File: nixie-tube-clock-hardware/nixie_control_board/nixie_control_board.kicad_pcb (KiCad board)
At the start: 2 copper layers, 72 x 97 mm, 66 parts, among them J1 Conn_01x07, J2 Conn_01x02_Female, P1 CONN_01X02, P2 CONN_01X02, P3 AMS1117, P5 ., Q1 IRF644, Q2 Q_PNP_BEC, SW1 SW_PUSH_SMALL, SW2 SW_PUSH_SMALL, SW3 SW_PUSH_SMALL, SW4 SW_DIP_x01, U1 DS3231, U2 AT24C02, U3 MAX1771, U4 Buzzer, U5 DHT11, U6 Logo, U7 SSD1306-OLED, U8 MP2307

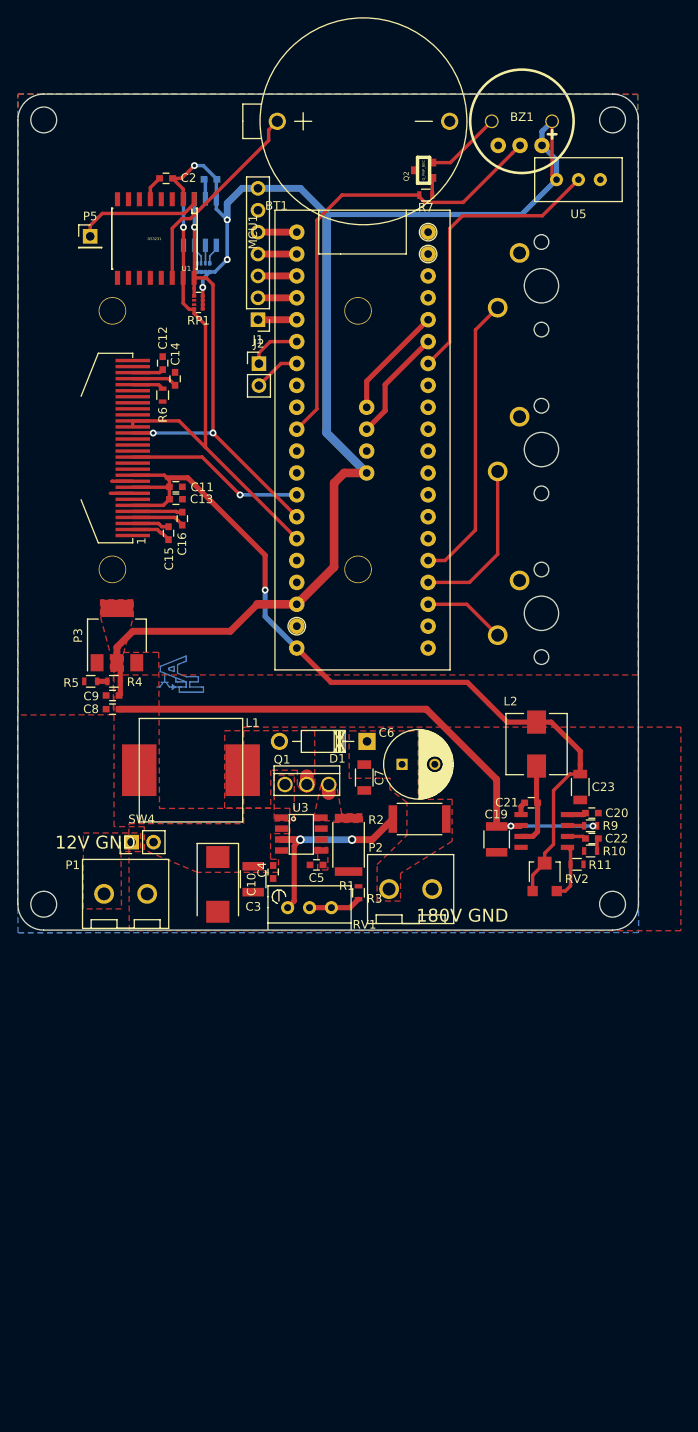
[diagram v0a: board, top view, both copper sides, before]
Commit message: Control board updated to encorporate 5v step down and 3.3v reg
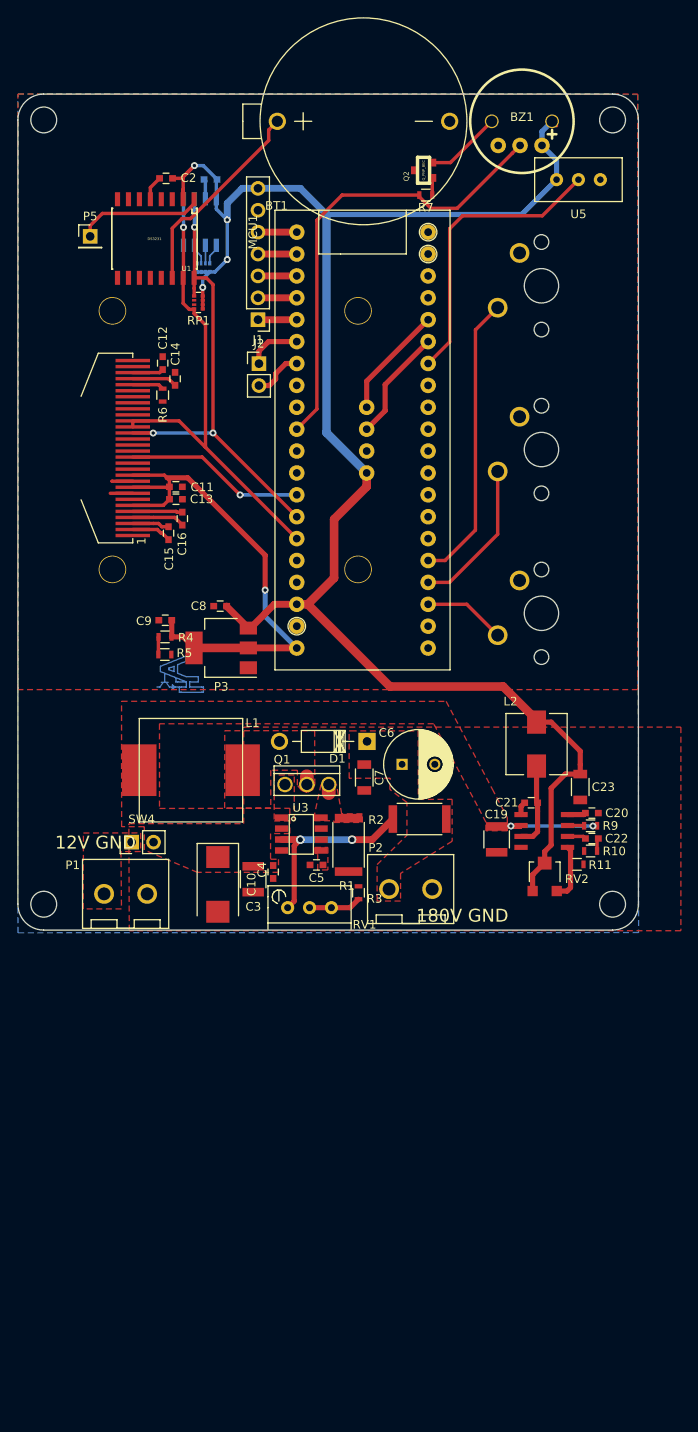
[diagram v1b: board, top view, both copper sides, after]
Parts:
- moved C8 17.3 mm to (136.5, 109.4)
- moved P3 12.2 mm to (136.6, 114.3), turned to 180 degrees
- moved C9 10.7 mm to (130.1, 111.0)
- moved R5 9.15 mm to (130.1, 115.0), turned to 0 degrees
- moved R4 7.87 mm to (130.1, 113.0)
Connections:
- C23 pad 2: +3V3 -> +5V
- C8 pad 1: +12V -> +5V
- C9 pad 1: +5V -> +3V3
- L2 pad 2: +3V3 -> +5V
- P3 pad 2: +5V -> +3V3
- P3 pad 3: +12V -> +5V
- P3 pad 4: (no net) -> +3V3
- R4 pad 1: +5V -> +3V3
- RV2 pad 1: +3V3 -> +5V
- RV2 pad 2: +3V3 -> +5V
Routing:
- net +12V: track 65.7 -> 13.0 mm
- net +3V3: track 100.0 -> 59.9 mm
- net +5V: track 171.9 -> 205.0 mm
- net BUTTON_2: track 19.0 -> 17.7 mm
- net Net-(R4-Pad2): track 1.18 -> 2.06 mm
- net BUZZER: track 53.2 -> 53.8 mm
- removed copper zone on F.Cu, net +5V

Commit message: Control board updated to be skinnier and ditch decondary through hole connections
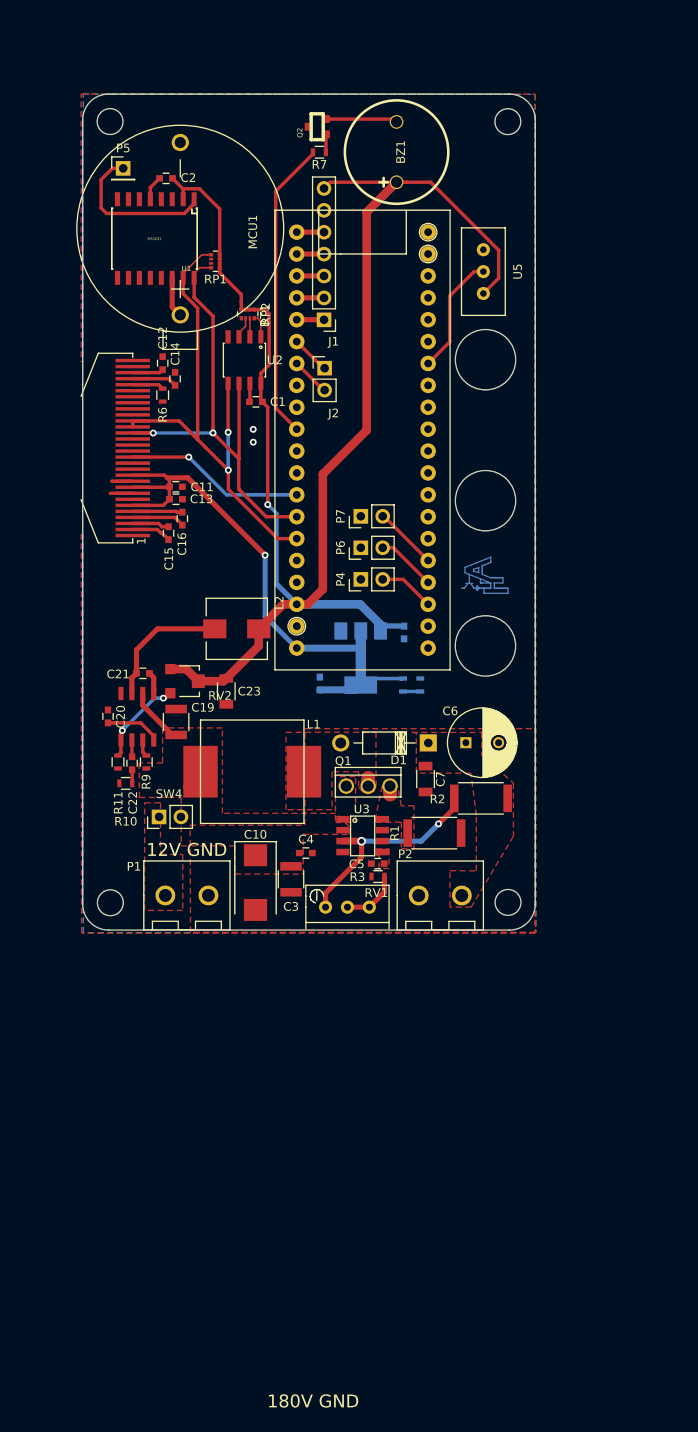
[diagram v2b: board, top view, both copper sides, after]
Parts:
- removed LCD1: 1.3_inch_LCD, keyboard:1.3_inch_LCD
- removed the REF** at (116.0, 53.0)
- removed the REF** at (116.0, 144.0)
- removed the REF** at (182.0, 144.0)
- removed SW1, SW2, SW3: SW_PUSH_SMALL, keyboard:CHERRY_PCB_100H
- removed U4: Buzzer, keyboard:Buzzer_shield
- added P4: CONN_01X02, Connector_PinHeader_2.54mm:PinHeader_1x02_P2.54mm_Vertical, F.Cu at (152.8, 106.3)
- added P6: CONN_01X02, Connector_PinHeader_2.54mm:PinHeader_1x02_P2.54mm_Vertical, F.Cu at (152.8, 102.6)
- added P7: CONN_01X02, Connector_PinHeader_2.54mm:PinHeader_1x02_P2.54mm_Vertical, F.Cu at (152.8, 99.0)
- added REF**: MountingHole_3mm, Mounting_Holes:MountingHole_3mm, F.Cu at (167.3, 97.2)
- added REF**: MountingHole_3mm, Mounting_Holes:MountingHole_3mm, F.Cu at (167.3, 80.8)
- added REF**: MountingHole_3mm, Mounting_Holes:MountingHole_3mm, F.Cu at (169.9, 143.8)
- added REF**: MountingHole_3mm, Mounting_Holes:MountingHole_3mm, F.Cu at (123.7, 143.8)
- added REF**: MountingHole_3mm, Mounting_Holes:MountingHole_3mm, F.Cu at (123.7, 53.2)
- added REF**: MountingHole_3mm, Mounting_Holes:MountingHole_3mm, F.Cu at (167.2, 114.0)
- C1, RP2, U2: moved to F.Cu
- C8, C9, P3, R4, R5: moved to B.Cu
- moved C20 57.2 mm to (123.5, 122.2), turned to 270 degrees
- moved R11 54.6 mm to (124.6, 127.5), turned to 90 degrees
- moved R10 54.5 mm to (125.5, 130.0)
- moved C22 54.1 mm to (126.2, 127.6), turned to 90 degrees
- moved R9 52.1 mm to (127.9, 127.5), turned to 270 degrees
- moved U8 49.0 mm to (126.9, 122.2), turned to 180 degrees
- moved RV2 47.6 mm to (132.3, 118.1), turned to 270 degrees
- moved C21 47.5 mm to (127.5, 117.2), turned to 0 degrees
- moved C23 42.5 mm to (137.2, 119.3)
- moved C19 39.6 mm to (131.4, 122.9), turned to 90 degrees
- moved L2 37.3 mm to (138.4, 112.0), turned to 0 degrees
- moved U6 37.2 mm to (168.9, 106.9)
- moved R5 29.9 mm to (159.7, 118.6), turned to 90 degrees
- moved R4 28.2 mm to (157.7, 118.6), turned to 270 degrees
- moved C1 26.3 mm to (140.6, 85.7)
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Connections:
- P2 pad 1: Net-(C6-Pad1) -> GND
- P2 pad 2: GND -> Net-(C6-Pad1)
- RP1 pad 5: SCL -> SDA
- RP1 pad 8: SDA -> SCL
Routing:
- net BUTTON_3: track 33.8 -> 7.39 mm
- net +5V: track 205.0 -> 178.7 mm, vias 4 -> 1
- net DHT: track 34.0 -> 13.9 mm
- net Net-(BT1-Pad1): track 23.8 -> 4.68 mm
- net BUZZER: track 53.8 -> 34.9 mm
- net SDA2: track 13.1 -> 0.00 mm
- net SCL2: track 13.1 -> 0.00 mm
- net BUTTON_2: track 17.7 -> 6.94 mm
- net +3V3: track 59.9 -> 68.8 mm
- net Net-(C21-Pad1): track 9.81 -> 15.4 mm
- net SDA: track 55.6 -> 60.9 mm, vias 1 -> 2
- net Net-(C20-Pad2): track 2.15 -> 6.40 mm
- net Net-(R11-Pad2): track 6.58 -> 10.5 mm, vias 0 -> 2
- net Net-(P5-Pad1): track 14.9 -> 18.4 mm
- net Net-(R2-Pad2): track 22.4 -> 25.0 mm
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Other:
- board size 72 x 97 mm -> 52.5 x 97 mm

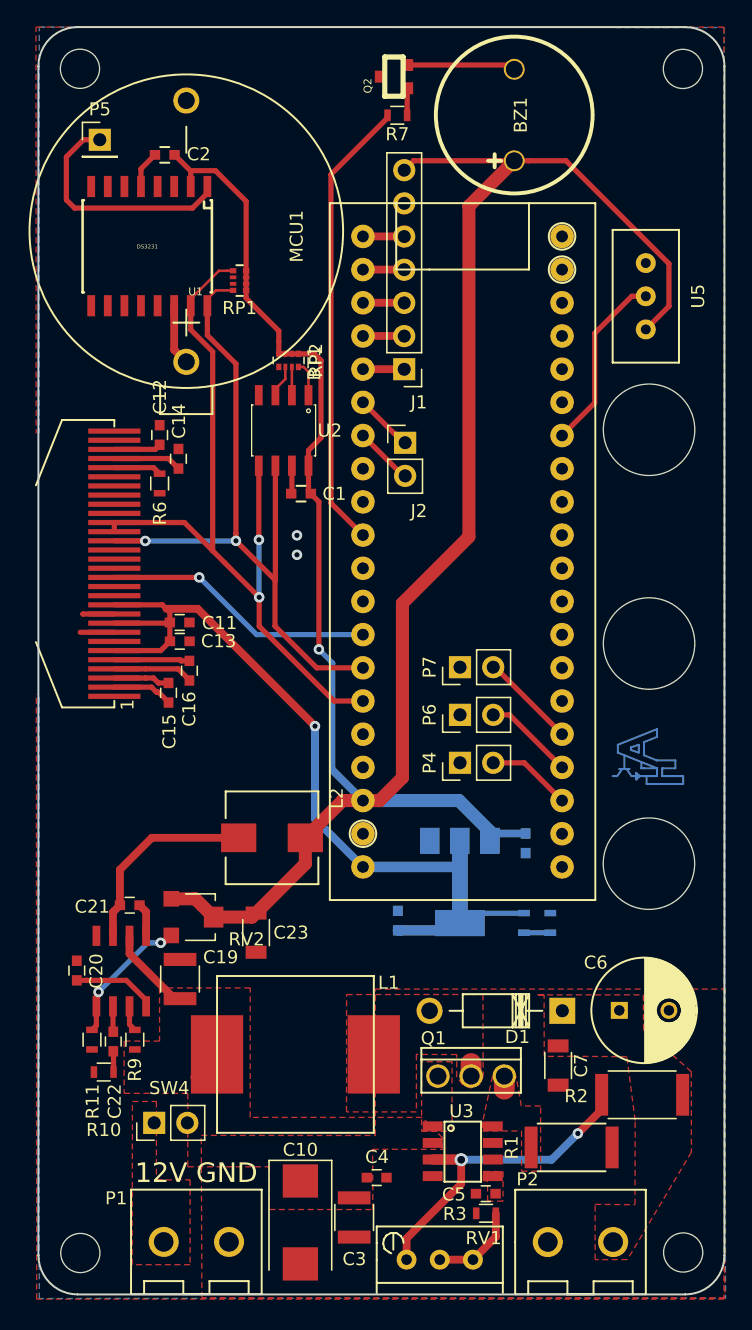
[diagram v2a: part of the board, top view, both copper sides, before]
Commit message: PCB Identifiers corrected
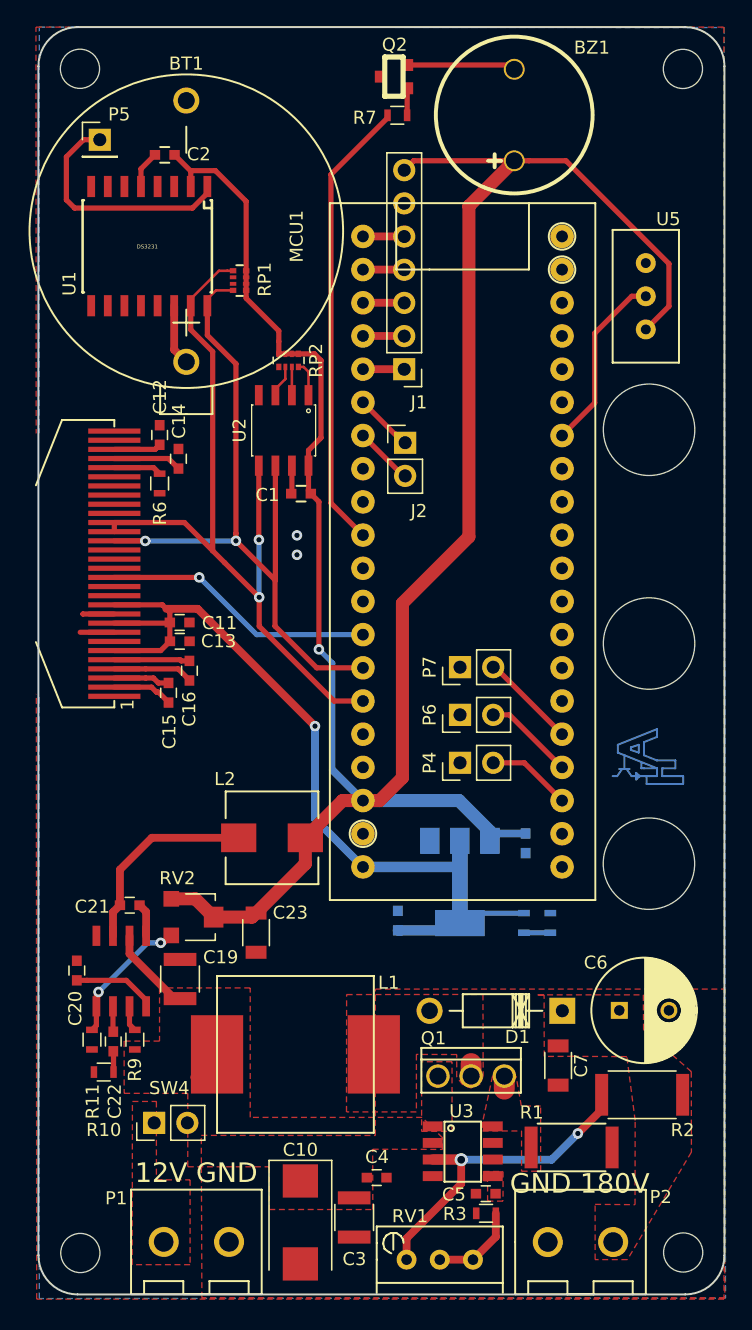
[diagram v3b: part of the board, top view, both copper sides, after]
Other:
- board text added: "GND 180V"

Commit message: control board gerber
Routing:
- net +12V: track 10.7 -> 11.9 mm
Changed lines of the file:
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@@
-(kicad_pcb (version 20171130) (host pcbnew 5.0.1)
+(kicad_pcb (version 20171130) (host pcbnew 5.1.5)
   (general
     (thickness 1.6)
     (drawings 13)
-    (tracks 252)
+    (tracks 253)
     (zones 0)
     (modules 67)
@@
   )
   (setup
-    (last_trace_width 0.2)
+    (last_trace_width 1.4)
     (user_trace_width 0.2)
     (user_trace_width 0.4)
@@
     (zone_45_only no)
     (trace_min 0.2)
-    (segment_width 0.2)
-    (edge_width 0.15)
     (via_size 0.8)
     (via_drill 0.4)
@@
     (uvia_min_size 0.2)
     (uvia_min_drill 0.1)
+    (edge_width 0.15)
+    (segment_width 0.2)
     (pcb_text_width 0.3)
     (pcb_text_size 1.5 1.5)
@@
     (visible_elements FFFFFF7F)
     (pcbplotparams
-      (layerselection 0x010fc_ffffffff)
+      (layerselection 0x010f0_ffffffff)
       (usegerberextensions true)
       (usegerberattributes false)
@@
       (creategerberjobfile false)
       (excludeedgelayer true)
-      (linewidth 0.100000)
+      (linewidth 0.150000)
       (plotframeref false)
       (viasonmask false)
@@
   (segment (start 127.49246 120.92722) (end 130.92524 124.36) (width 0.6) (layer F.Cu) (net 39))
   (segment (start 127.49246 119.55252) (end 127.49246 120.92722) (width 0.6) (layer F.Cu) (net 39))
+  (segment (start 131.92 133.87) (end 133.095 133.87) (width 1.4) (layer F.Cu) (net 39))
   (segment (start 163.1 73.43237) (end 163.1 78.76) (width 0.4) (layer F.Cu) (net 40))
   (segment (start 165.93237 70.6) (end 163.1 73.43237) (width 0.4) (layer F.Cu) (net 40))
@@
     (connect_pads (clearance 0.5))
     (min_thickness 0.03)
-    (fill (arc_segments 16) (thermal_gap 0.508) (thermal_bridge_width 0.508) (smoothing fillet) (radius 0.3))
+    (fill yes (arc_segments 16) (thermal_gap 0.508) (thermal_bridge_width 0.508) (smoothing fillet) (radius 0.3))
     (polygon
       (pts
@@
     (connect_pads (clearance 0.5))
     (min_thickness 0.03)
-    (fill (arc_segments 16) (thermal_gap 0.508) (thermal_bridge_width 0.508) (smoothing fillet) (radius 0.3))
+    (fill yes (arc_segments 16) (thermal_gap 0.508) (thermal_bridge_width 0.508) (smoothing fillet) (radius 0.3))
     (polygon
       (pts
@@
     (connect_pads (clearance 0.5))
     (min_thickness 0.03)
-    (fill (arc_segments 16) (thermal_gap 0.508) (thermal_bridge_width 0.508) (smoothing fillet) (radius 0.3))
+    (fill yes (arc_segments 16) (thermal_gap 0.508) (thermal_bridge_width 0.508) (smoothing fillet) (radius 0.3))
     (polygon
       (pts
@@
     (connect_pads (clearance 0.5))
     (min_thickness 0.03)
-    (fill (arc_segments 16) (thermal_gap 0.508) (thermal_bridge_width 0.508) (smoothing fillet) (radius 0.3))
+    (fill yes (arc_segments 16) (thermal_gap 0.508) (thermal_bridge_width 0.508) (smoothing fillet) (radius 0.3))
     (polygon
       (pts
@@
     (connect_pads (clearance 0.5))
     (min_thickness 0.03)
-    (fill (arc_segments 16) (thermal_gap 0.508) (thermal_bridge_width 0.508) (smoothing fillet) (radius 0.5))
+    (fill yes (arc_segments 16) (thermal_gap 0.508) (thermal_bridge_width 0.508) (smoothing fillet) (radius 0.5))
     (polygon
       (pts
@@
     (connect_pads (clearance 0.5))
     (min_thickness 0.03)
-    (fill (arc_segments 16) (thermal_gap 0.508) (thermal_bridge_width 0.508) (smoothing fillet) (radius 0.5))
+    (fill yes (arc_segments 16) (thermal_gap 0.508) (thermal_bridge_width 0.508) (smoothing fillet) (radius 0.5))
     (polygon
       (pts
@@
     (connect_pads (clearance 0.4))
     (min_thickness 0.15)
-    (fill (arc_segments 16) (thermal_gap 0.508) (thermal_bridge_width 0.508) (smoothing fillet) (radius 0.5))
+    (fill yes (arc_segments 16) (thermal_gap 0.508) (thermal_bridge_width 0.508) (smoothing fillet) (radius 0.5))
     (polygon
       (pts
@@
     (connect_pads thru_hole_only (clearance 0.4))
     (min_thickness 0.254)
-    (fill (arc_segments 16) (thermal_gap 0.508) (thermal_bridge_width 0.508))
+    (fill yes (arc_segments 16) (thermal_gap 0.508) (thermal_bridge_width 0.508))
     (polygon
       (pts
@@
     (connect_pads (clearance 0.5))
     (min_thickness 0.03)
-    (fill (arc_segments 16) (thermal_gap 0.508) (thermal_bridge_width 0.508) (smoothing fillet) (radius 0.3))
+    (fill yes (arc_segments 16) (thermal_gap 0.508) (thermal_bridge_width 0.508) (smoothing fillet) (radius 0.3))
     (polygon
       (pts
@@
     (connect_pads (clearance 0.4))
     (min_thickness 0.254)
-    (fill (arc_segments 16) (thermal_gap 0.508) (thermal_bridge_width 0.508))
+    (fill yes (arc_segments 16) (thermal_gap 0.508) (thermal_bridge_width 0.508))
     (polygon
       (pts

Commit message: Clean up
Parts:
- C1: value C_Small -> 1uF; footprint Capacitors_SMD:C_0603 -> Capacitor_SMD:C_0603_1608Metric
- C10: footprint Capacitors_Tantalum_SMD:CP_Tantalum_Case-V_EIA-7343-20_Reflow -> Capacitor_Tantalum_SMD:CP_EIA-7343-15_Kemet-W
- C11, C13, C15, C16: value C -> 1uF; footprint Capacitors_SMD:C_0603 -> Capacitor_SMD:C_0603_1608Metric
- C12, C8: value C -> 10uF; footprint Capacitors_SMD:C_0603 -> Capacitor_SMD:C_0603_1608Metric
- C14: value C -> 2.2uF/16V; footprint Capacitors_SMD:C_0603 -> Capacitor_SMD:C_0603_1608Metric
- C19, C3: footprint Capacitors_SMD:C_1210 -> Capacitor_SMD:C_1210_3225Metric
- C2: value C_Small -> 0.1uF; footprint Capacitors_SMD:C_0603 -> Capacitor_SMD:C_0603_1608Metric
- C20, C21, C22: footprint Capacitors_SMD:C_0603 -> Capacitor_SMD:C_0603_1608Metric
- C23, C7: footprint Capacitors_SMD:C_1206 -> Capacitor_SMD:C_1206_3216Metric
- C4, C5: footprint Capacitors_SMD:C_0603 -> Capacitor_SMD:C_0805_2012Metric
- C9: value CP1 -> 10uF; footprint Capacitors_SMD:C_0603 -> Capacitor_SMD:C_0603_1608Metric
- P5: footprint Pin_Headers:Pin_Header_Straight_1x01_Pitch2.54mm -> Connector_PinHeader_2.54mm:PinHeader_1x01_P2.54mm_Vertical
- R4, R5: value R -> 0
- R6: value R -> 390K
- R7: value R -> 1K
- moved C10 0.90 mm to (140.7, 142.4)
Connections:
- R4 pad 2: Net-(R4-Pad2) -> GND
- R5 pad 1: Net-(R4-Pad2) -> GND
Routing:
- net Net-(R4-Pad2): track 2.02 -> 0.00 mm
- net GND: track 10.0 -> 12.1 mm
